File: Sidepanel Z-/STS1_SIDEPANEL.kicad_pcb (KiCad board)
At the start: 4 copper layers, 82.8 x 100 mm, 32 parts, among them IC1 TMP112AQDRLRQ1, J1 Conn_01x18, J3 Conn_01x12, U1 GUVA-C32SM, U11 INA180A4

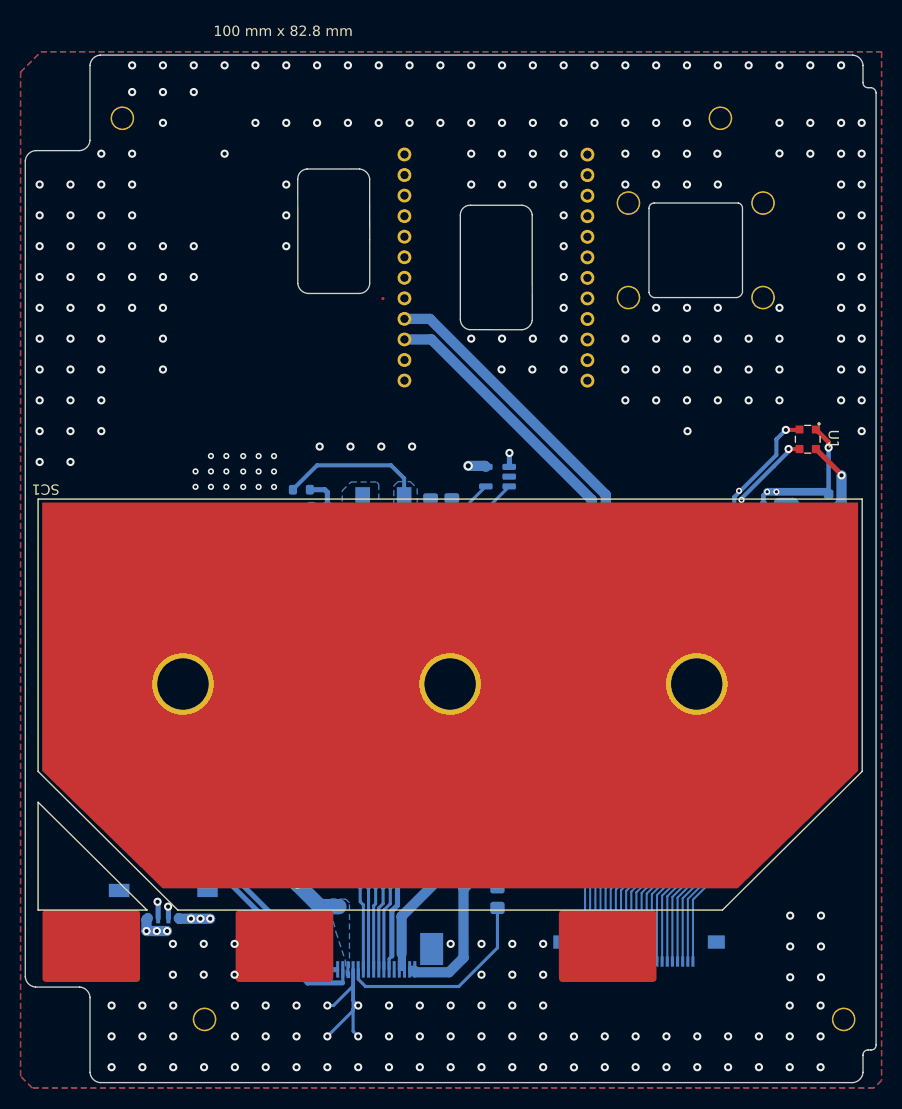
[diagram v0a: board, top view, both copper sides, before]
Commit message: changed all vias from blind to trough and removed the unused pins of the uci connector
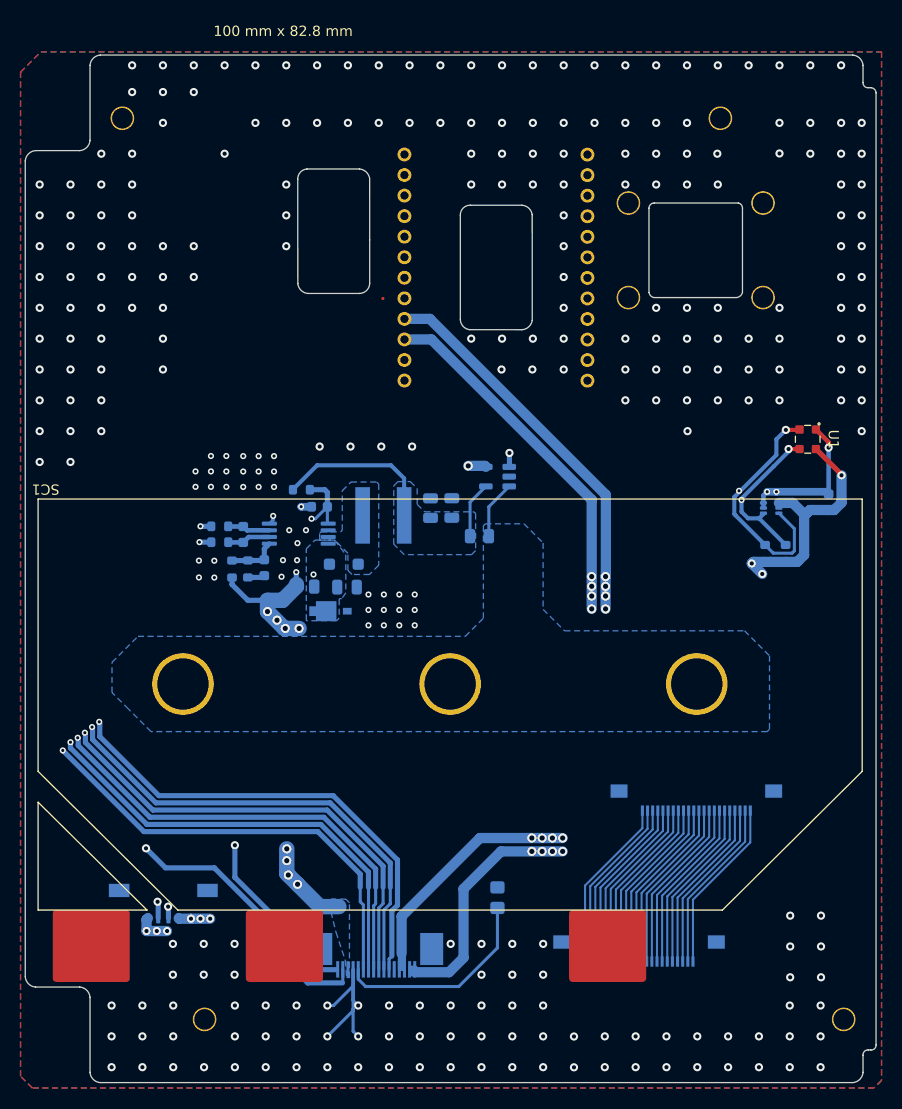
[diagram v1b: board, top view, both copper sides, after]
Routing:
- net /SDA: track 106.9 -> 114.4 mm
- net GND1: track 100.5 -> 107.9 mm
- net /SCL: track 97.5 -> 104.9 mm
- net /+3V3: track 109.8 -> 114.2 mm

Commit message: chaned the connectors for the cameras from buttom to top contact
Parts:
- cam1: value 54548-2271 -> 52435-2271; footprint STS_connector:545482271 -> STS_connector:524352271
- moved cam1 0.41 mm to (148.9, 110.6)
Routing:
- net GND: vias 291 -> 288

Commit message: connected the vias for the solar cell together
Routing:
- net /SC1_V+: track 41.6 -> 91.6 mm
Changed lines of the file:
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@@
 		(fp_arc
 			(start 1.842927 -23.275957)
-			(mid 1.206593 -23.605054)
+			(mid 1.206596 -23.605055)
 			(end 0.94 -24.27)
 			(stroke
@@
 		(fp_arc
 			(start 7.937653 -24.17174)
-			(mid 7.59436 -23.548792)
+			(mid 7.594362 -23.548791)
 			(end 6.94 -23.27)
 			(stroke
@@
 		(fp_arc
 			(start 28.4 -26.9)
-			(mid 28.190731 -26.563652)
+			(mid 28.190734 -26.56367)
 			(end 27.83 -26.4)
 			(stroke
@@
 			(pintype "passive+no_connect")
 		)
-		(model "52435-2271.stp"
+		(model "/home/stefan/DEV/spaceteam/STS1_PCB_SIDEPANEL/libs/3d/STS_Connector/52435-2271.stp"
 			(offset
-				(xyz 0 2.099999873 0.04999999999)
+				(xyz 0 -1.4 -0.45)
 			)
 			(scale
@@
 			)
 			(rotate
-				(xyz -90 0 0)
+				(xyz 0 0 0)
 			)
 		)
@@
 	)
 	(segment
+		(start 124.9492 100.7098)
+		(end 148.9492 100.7098)
+		(width 2)
+		(layer "F.Cu")
+		(net 8)
+	)
+	(segment
 		(start 149.0442 100.8048)
 		(end 148.9492 100.7098)
@@
 		(layer "F.Cu")
 		(net 8)
+	)
+	(segment
+		(start 124.9492 100.7098)
+		(end 98.9492 100.7098)
+		(width 2)
+		(layer "F.Cu")
+		(net 8)

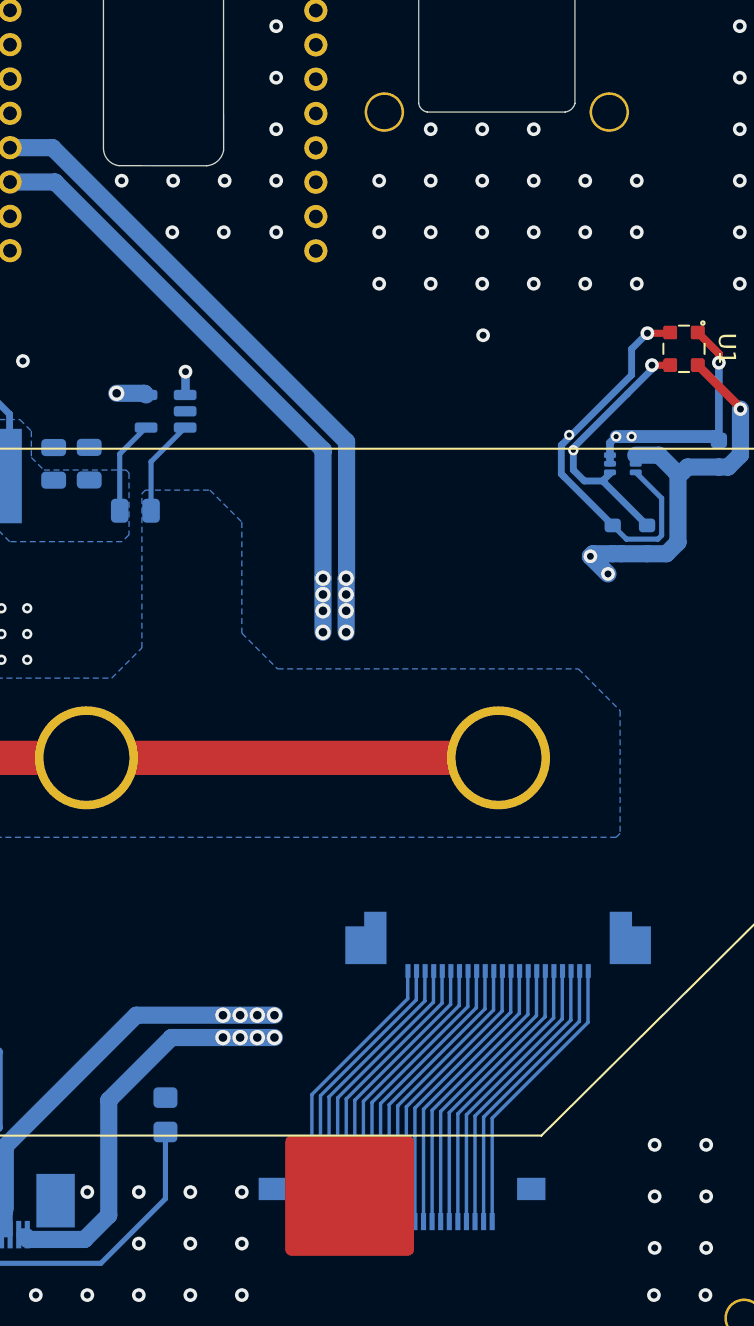
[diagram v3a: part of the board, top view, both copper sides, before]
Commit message: moved the camera connectors to be sure that the cable can be inserted
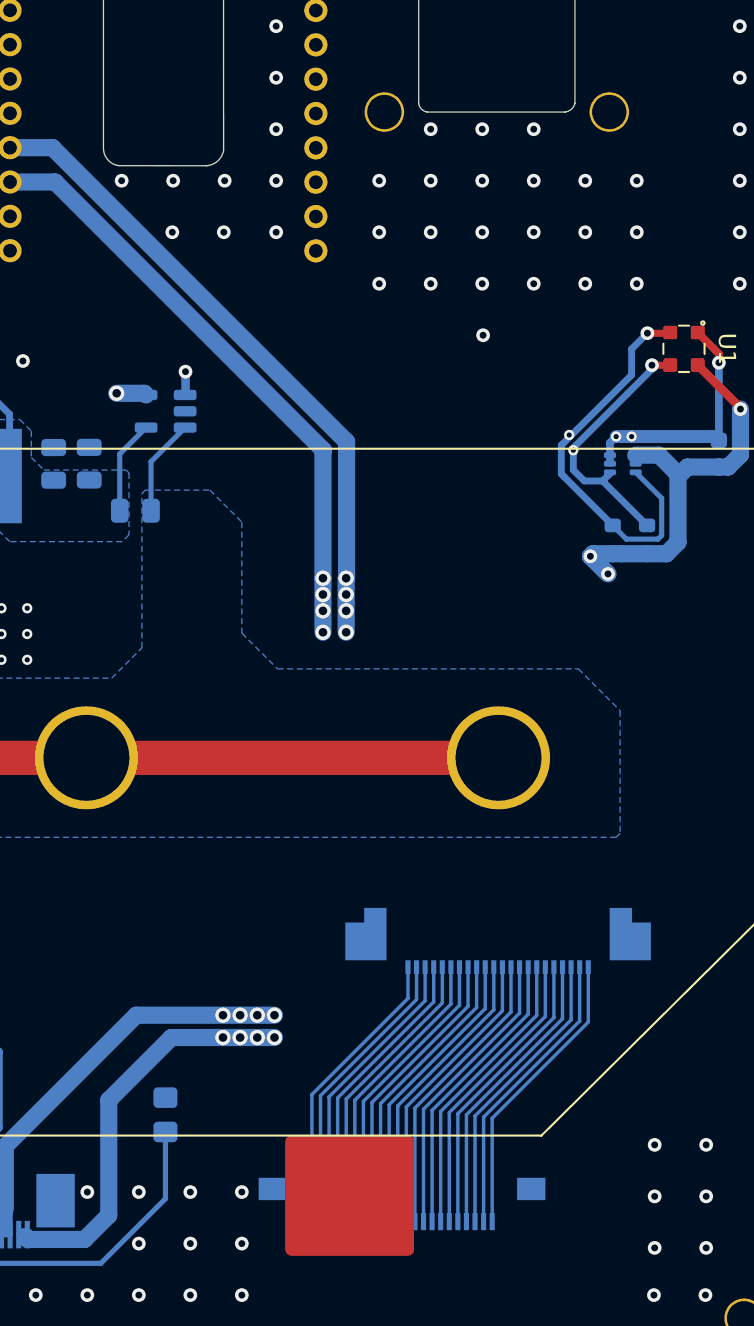
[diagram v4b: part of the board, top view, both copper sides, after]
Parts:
- moved cam1 0.23 mm to (148.9, 110.3)

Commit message: Removed some  unnecessary drawings from the silkscreen.
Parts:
- moved cam1 0.40 mm to (148.9, 110.0)
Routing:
- net GND: vias 288 -> 292

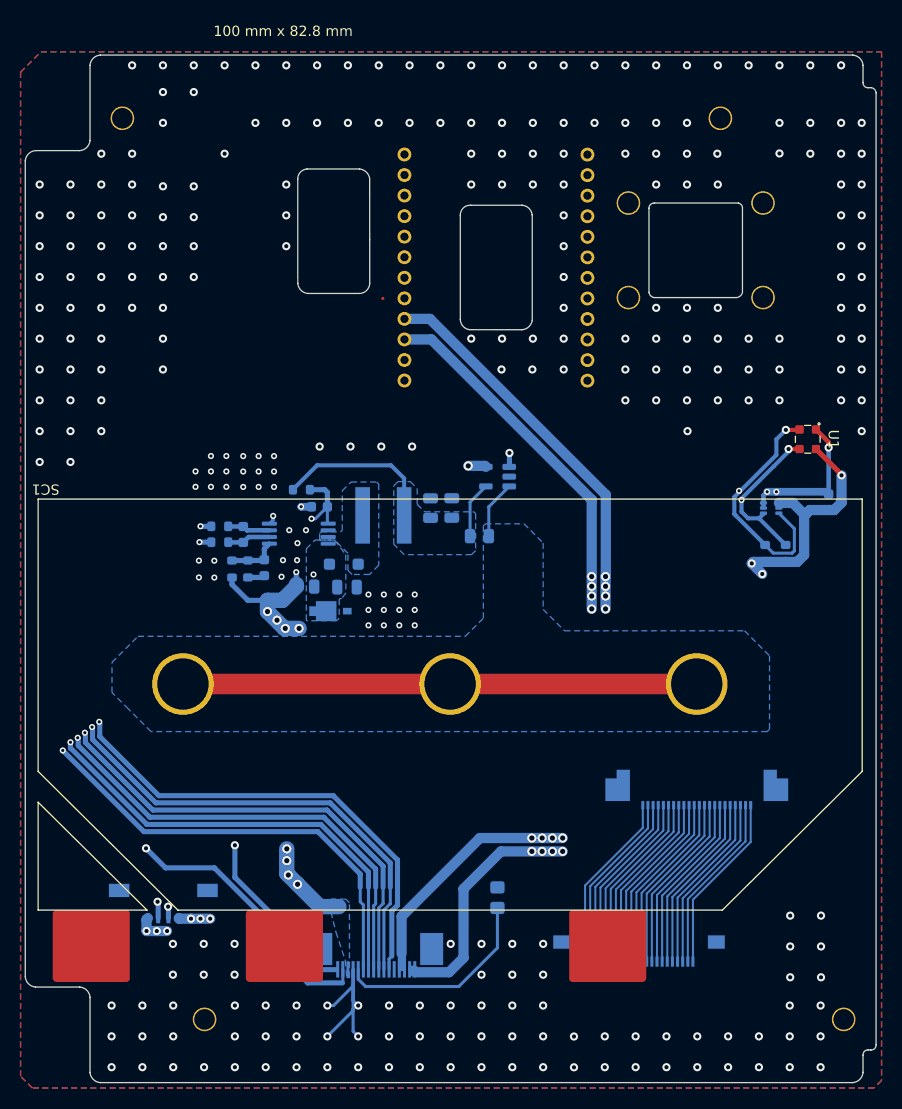
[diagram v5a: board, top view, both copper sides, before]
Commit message: Generated the gerber files and moved some vias around.
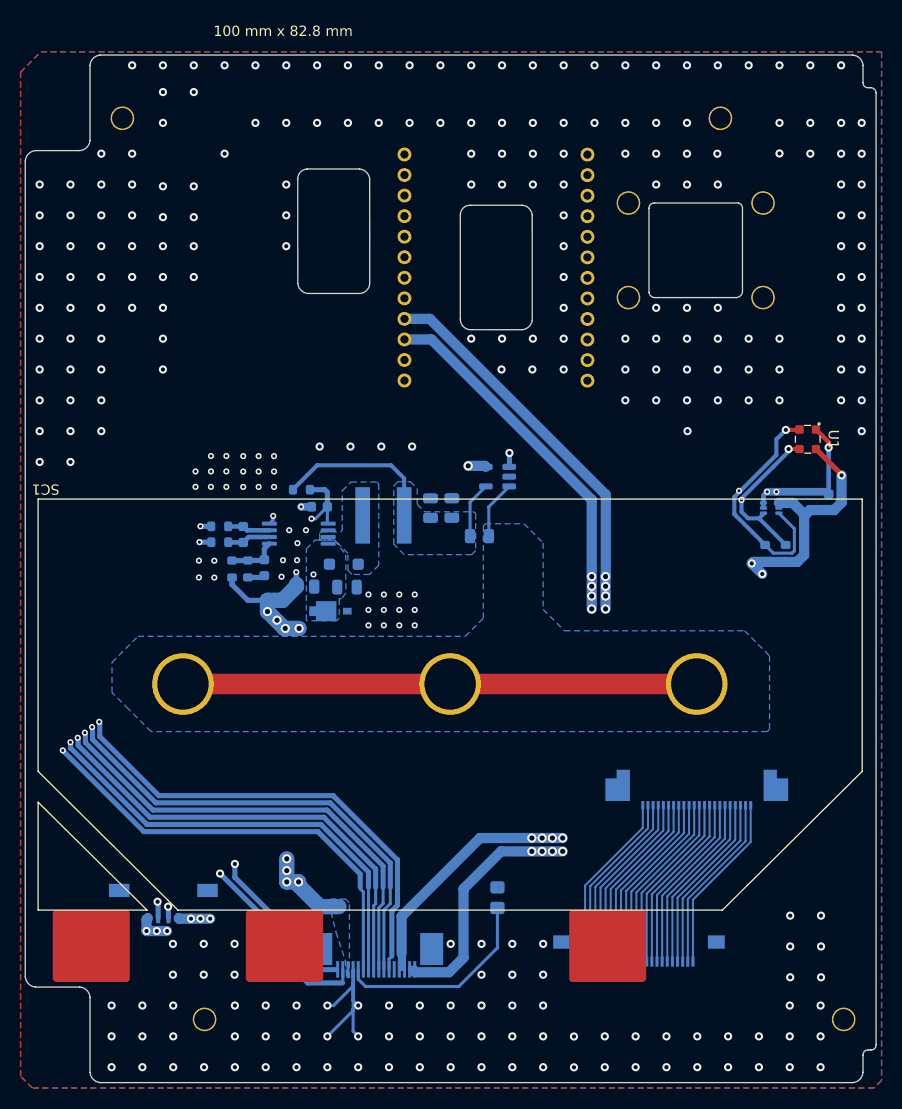
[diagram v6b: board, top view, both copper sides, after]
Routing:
- net /SC1_I+: track 102.1 -> 99.3 mm
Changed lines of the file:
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@@
 		(fp_arc
 			(start 1.842927 -23.275957)
-			(mid 1.206595 -23.605056)
+			(mid 1.206596 -23.605055)
 			(end 0.94 -24.27)
 			(stroke
@@
 		(fp_arc
 			(start 7.937653 -24.17174)
-			(mid 7.594359 -23.548796)
+			(mid 7.594355 -23.548799)
 			(end 6.94 -23.27)
 			(stroke
@@
 		(fp_arc
 			(start 28.4 -26.9)
-			(mid 28.190731 -26.563652)
+			(mid 28.190721 -26.563683)
 			(end 27.83 -26.4)
 			(stroke
@@
 		)
 	)
-	(segment
-		(start 118.4134 63.1866)
-		(end 118.4 63.2)
-		(width 0.3)
-		(layer "F.Cu")
-		(net 1)
-	)
 	(via
 		(at 163 61.1)
@@
 	)
 	(via
-		(at 104 116.4)
+		(at 104 118.22)
 		(size 0.8)
 		(drill 0.4)
@@
 	)
 	(segment
-		(start 104 116.4)
+		(start 104 118.22)
 		(end 104 105.7606)
 		(width 0.5)
@@
 	)
 	(segment
-		(start 110.788001 128.51)
-		(end 113.905 128.51)
+		(start 130.6975 81.4775)
+		(end 128.7125 83.4625)
+		(width 0.3)
+		(layer "B.Cu")
+		(net 8)
+	)
+	(segment
+		(start 109.65 125.175)
+		(end 109.65 127.371999)
 		(width 0.5)
 		(layer "B.Cu")
@@
 	)
 	(segment
-		(start 130.6975 81.4775)
-		(end 128.7125 83.4625)
-		(width 0.3)
+		(start 104 118.22)
+		(end 104 119.525)
+		(width 0.5)
 		(layer "B.Cu")
 		(net 8)
@@
 	)
 	(segment
-		(start 104 116.4)
-		(end 104 119.525)
-		(width 0.5)
-		(layer "B.Cu")
-		(net 8)
-	)
-	(segment
-		(start 109.65 125.175)
-		(end 109.65 127.371999)
+		(start 110.788001 128.51)
+		(end 113.905 128.51)
 		(width 0.5)
 		(layer "B.Cu")
@@
 	)
 	(via
-		(at 95.35 116.7)
+		(at 102.555 119.155)
 		(size 0.8)
 		(drill 0.4)
@@
 	)
 	(segment
-		(start 129.23 76.73)
-		(end 130.72 78.22)
+		(start 94.15 110.75)
+		(end 94.15 83.66)
 		(width 0.5)
 		(layer "In2.Cu")
@@
 	)
 	(segment
-		(start 95.35 116.7)
-		(end 94.15 115.5)
+		(start 129.23 76.73)
+		(end 130.72 78.22)
 		(width 0.5)
 		(layer "In2.Cu")
@@
 	)
 	(segment
-		(start 94.15 115.5)
-		(end 94.15 83.66)
+		(start 102.555 119.155)
+		(end 94.15 110.75)
 		(width 0.5)
 		(layer "In2.Cu")
@@
 	)
 	(segment
-		(start 108.95 125.55)
-		(end 108.95 127.661949)
-		(width 0.5)
-		(layer "B.Cu")
-		(net 9)
-	)
-	(segment
-		(start 108.95 127.661949)
-		(end 111.088051 129.8)
+		(start 111.088051 129.8)
+		(end 114.475 129.8)
 		(width 0.5)
 		(layer "B.Cu")
@@
 	)
 	(segment
-		(start 111.088051 129.8)
-		(end 114.475 129.8)
+		(start 102.555 119.155)
+		(end 108.95 125.55)
 		(width 0.5)
 		(layer "B.Cu")
@@
 	)
 	(segment
-		(start 95.35 116.7)
-		(end 97.25 118.6)
-		(width 0.5)
-		(layer "B.Cu")
-		(net 9)
-	)
-	(segment
-		(start 102 118.6)
-		(end 108.95 125.55)
+		(start 108.95 125.55)
+		(end 108.95 127.661949)
 		(width 0.5)
 		(layer "B.Cu")
@@
 	)
 	(segment
-		(start 97.25 118.6)
-		(end 102 118.6)
+		(start 108.95 127.661949)
+		(end 111.088051 129.8)
 		(width 0.5)
 		(layer "B.Cu")
@@
 	)
 	(via
-		(at 110.1 120.2)
+		(at 110.2 119.97)
 		(size 0.9)
 		(drill 0.5)
@@
 	)
 	(via
-		(at 109.05 116.75)
+		(at 109.05 117.719997)
 		(size 0.9)
 		(drill 0.5)
@@
 	)
 	(via
-		(at 109.05 117.9)
+		(at 109.05 118.87)
 		(size 0.9)
 		(drill 0.5)
@@
 	)
 	(via
-		(at 109.2 119.3)
+		(at 109.05 119.97)
 		(size 0.9)
 		(drill 0.5)
@@
 	)
 	(segment
-		(start 109.1 119.2)
-		(end 110.1 120.2)
-		(width 1.5)
-		(layer "In2.Cu")
-		(net 10)
-	)
-	(segment
-		(start 109.1 95.585)
-		(end 109.1 119.2)
-		(width 1.5)
-		(layer "In2.Cu")
-		(net 10)
-	)
-	(segment
 		(start 110 89.85)
 		(end 109.975 89.825)
@@
 	)
 	(segment
+		(start 109.1 119.92)
+		(end 109.1 95.585)
+		(width 1.5)
+		(layer "In2.Cu")
+		(net 10)
+	)
+	(segment
 		(start 109.385 95.3)
 		(end 109.1 95.585)
@@
 	)
 	(segment
+		(start 109.05 119.97)
+		(end 109.1 119.92)
+		(width 1.5)
+		(layer "In2.Cu")
+		(net 10)
+	)
+	(segment
+		(start 110.2 119.97)
+		(end 109.05 119.97)
+		(width 1.5)
+		(layer "In2.Cu")
+		(net 10)
+	)
+	(segment
 		(start 109.99 91.015)
 		(end 109.99 91.21)
@@
 	)
 	(segment
-		(start 109.2 119.3)
-		(end 109.05 119.15)
+		(start 112.275 122.375)
+		(end 114.125 122.375)
 		(width 1.5)
 		(layer "B.Cu")
@@
 	)
 	(segment
-		(start 110.1 120.2)
-		(end 109.2 119.3)
+		(start 109.05 119.97)
+		(end 109.05 117.719997)
 		(width 1.5)
 		(layer "B.Cu")
@@
 	)
 	(segment
-		(start 107.175 93.66)
-		(end 107.175 92.565)
+		(start 110.2 119.97)
+		(end 109.05 119.97)
 		(width 1.5)
 		(layer "B.Cu")
@@
 	)
 	(segment
-		(start 112.275 122.375)
-		(end 114.125 122.375)
+		(start 107.175 93.66)
+		(end 107.175 92.565)
 		(width 1.5)
 		(layer "B.Cu")
@@
 	)
 	(segment
+		(start 110.2 119.97)
+		(end 110.2 120.3)
+		(width 1.5)
+		(layer "B.Cu")
+		(net 10)
+	)
+	(segment
 		(start 108.635 92.565)
 		(end 107.175 92.565)
@@
 	)
 	(segment
-		(start 109.05 119.15)
-		(end 109.05 116.75)
-		(width 1.5)
-		(layer "B.Cu")
-		(net 10)
-	)
-	(segment
-		(start 112.275 122.375)
-		(end 110.1 120.2)
-		(width 1.5)
-		(layer "B.Cu")
-		(net 10)
-	)
-	(segment
 		(start 110.25 95.3)
 		(end 108.815 95.3)
@@
 	)
 	(segment
+		(start 110.2 120.3)
+		(end 112.275 122.375)
+		(width 1.5)
+		(layer "B.Cu")
+		(net 10)
+	)
+	(segment
 		(start 109.975 89.825)
 		(end 109.975 91)
@@
 	)
 	(segment
+		(start 116.2 120.64)
+		(end 116.2 120.5)
+		(width 0.3)
+		(layer "B.Cu")
+		(net 40)
+	)
+	(segment
 		(start 116.505 128.48)
-		(end 116.505 122.205)
+		(end 116.505 120.945)
 		(width 0.3)
 		(layer "B.Cu")
@@
 	)
 	(segment
-		(start 116.505 122.205)
-		(end 116.2 121.9)
+		(start 116.505 120.945)
+		(end 116.2 120.64)
 		(width 0.3)
 		(layer "B.Cu")
@@
 		(layer "B.Cu")
 		(net 40)
-	)
-	(segment
-		(start 116.2 121.9)
-		(end 116.2 120.5)
-		(width 0.3)
-		(layer "B.Cu")
-		(net 40)
